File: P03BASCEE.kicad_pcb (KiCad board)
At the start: 2 copper layers, 39.6 x 37.6 mm, 21 parts, among them J1 Serial, J2 Digital, J3 ICSP, J4 I2C, U1 24LC1025, U2 24LC1025, U3 DS13375+, U4 ATMEGA328P-AU, Y1 Crystal 32MHz, Y2 Crystal 16MHz

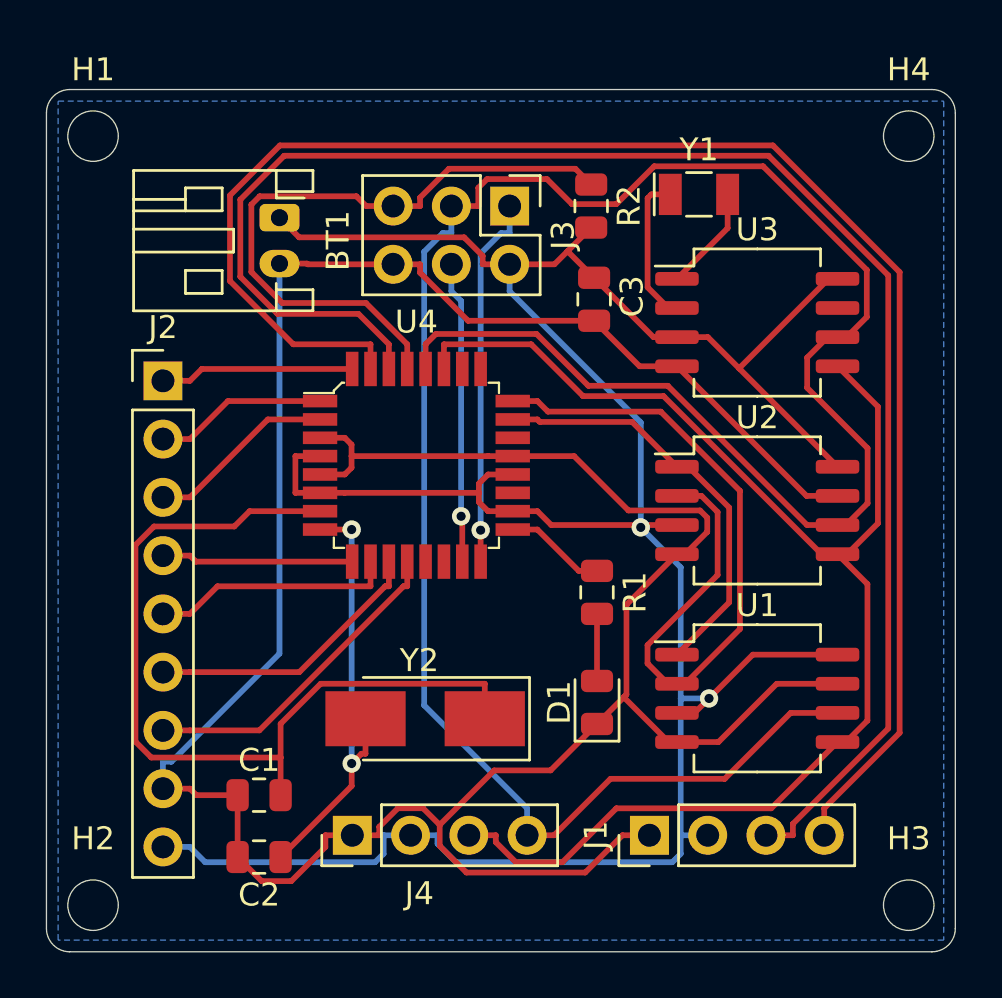
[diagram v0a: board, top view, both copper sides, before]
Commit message: Modificatos silkscreens para projeto duas camadas e adicionadas dimensões
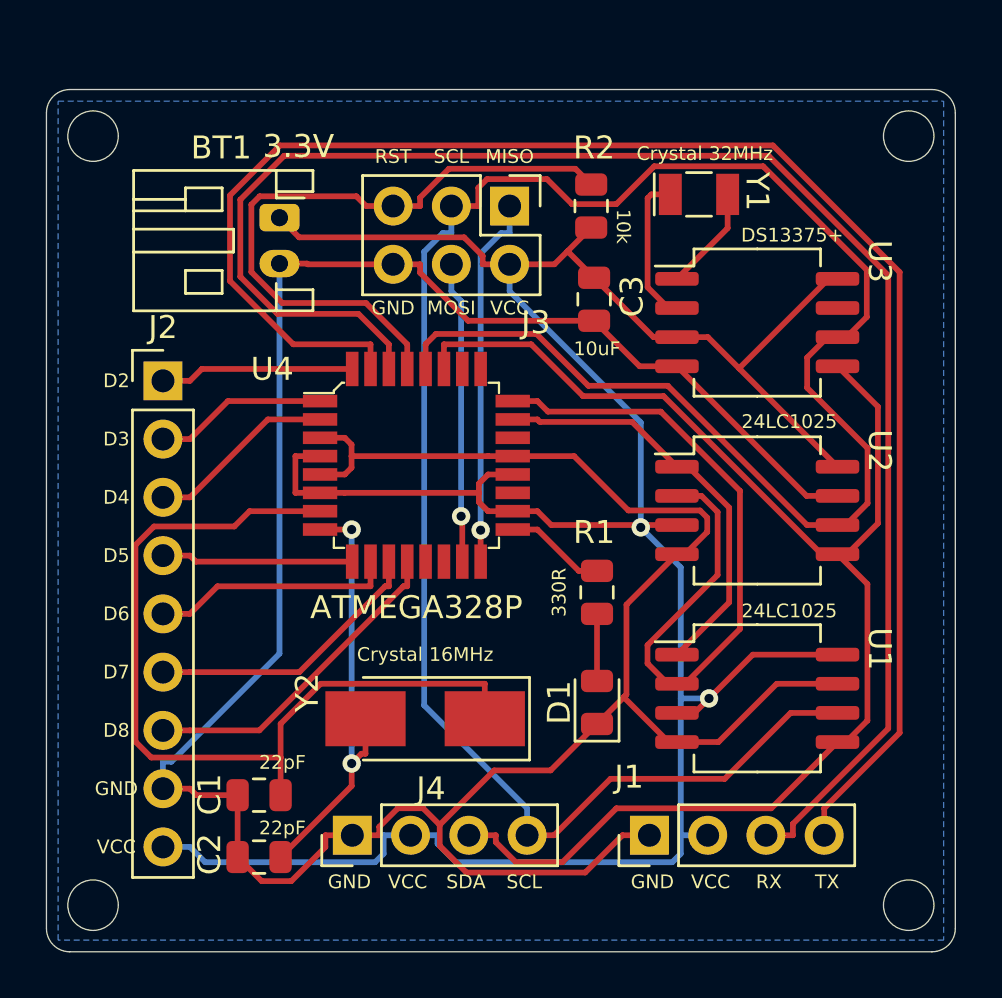
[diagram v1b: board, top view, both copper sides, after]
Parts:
- added G***: LOGO, logo_UFS:logo_UFS_grande, B.Cu at (153.1, 116.3)
- added REF**: KiCad-Logo2_5mm_SilkScreen, Symbol:KiCad-Logo2_5mm_SilkScreen, B.Cu at (149.2, 106.7)
- U4: value ATMEGA328P-AU -> ATMEGA328P
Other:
- board text added: "3.3V"
- board text added: "BACEE v1.0 Designed by Raphael Cardoso cardosodeoliveir@gmail.com"
- board text added: "D2"
- board text added: "D3"
- board text added: "D4"
- board text added: "D5"
- board text added: "D6"
- board text added: "D7"
- board text added: "D8"
- board text added: "GND"
- board text added: "MISO"
- board text added: "MOSI"
- board text added: "RST"
- board text added: "RX"
- board text added: "SCL"
- board text added: "SDA"
- board text added: "TX"
- board text added: "VCC"
